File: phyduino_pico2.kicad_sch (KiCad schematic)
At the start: 7 parts, among them J2 PM2.54-1*8, J3 PM2.54-1*10, J4 PM2.54-1*6, J5 PM2.54-1*8, J7 HC-FPC-0.5-22P-CSH20

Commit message: Built board without USB-PD variant. Not yet complete.
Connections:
- net Microcontroller/HS_I2C0_SCL renamed Microcontroller/HS_I2C1_SCL
- net Microcontroller/HS_I2C0_SDA renamed Microcontroller/HS_I2C1_SDA
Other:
- sheet Microcontroller ports: added HS_I2C1_SCL, HS_I2C1_SDA; removed HS_I2C0_SCL, HS_I2C0_SDA
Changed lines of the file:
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@@
+			)
+		)
+		(property "Tolerance" ""
+			(at 300.99 256.54 0)
+			(hide yes)
+			(show_name no)
+			(do_not_autoplace no)
+			(effects
+				(font
+					(size 1.27 1.27)
+				)
 			)
 		)
@@
 			)
 		)
+		(property "Tolerance" ""
+			(at 295.91 256.54 0)
+			(hide yes)
+			(show_name no)
+			(do_not_autoplace no)
+			(effects
+				(font
+					(size 1.27 1.27)
+				)
+			)
+		)
 		(instances
 			(project "phyduino_pico2"
@@
 			)
 		)
+		(property "Tolerance" ""
+			(at 237.49 87.63 0)
+			(hide yes)
+			(show_name no)
+			(do_not_autoplace no)
+			(effects
+				(font
+					(size 1.27 1.27)
+				)
+			)
+		)
 		(pin "1"
 		)
@@
 			)
 		)
+		(property "Tolerance" ""
+			(at 237.49 137.16 0)
+			(hide yes)
+			(show_name no)
+			(do_not_autoplace no)
+			(effects
+				(font
+					(size 1.27 1.27)
+				)
+			)
+		)
 		(pin "13"
 		)
@@
 		)
 		(property "KiLib_Generator" "connector/pin_header_socket"
+			(at 237.49 62.23 0)
+			(hide yes)
+			(show_name no)
+			(do_not_autoplace no)
+			(effects
+				(font
+					(size 1.27 1.27)
+				)
+			)
+		)
+		(property "Tolerance" ""
 			(at 237.49 62.23 0)
 			(hide yes)
@@
 		)
 		(property "KiLib_Generator" "connector/pin_header_socket"
+			(at 40.64 62.23 0)
+			(hide yes)
+			(show_name no)
+			(do_not_autoplace no)
+			(effects
+				(font
+					(size 1.27 1.27)
+				)
+			)
+		)
+		(property "Tolerance" ""
 			(at 40.64 62.23 0)
 			(hide yes)
@@
 			)
 		)
+		(property "Tolerance" ""
+			(at 237.49 181.61 0)
+			(hide yes)
+			(show_name no)
+			(do_not_autoplace no)
+			(effects
+				(font
+					(size 1.27 1.27)
+				)
+			)
+		)
 		(pin "1"
 		)
@@
 			)
 		)
-		(pin "HS_I2C0_SCL" bidirectional
+		(pin "HS_I2C1_SCL" bidirectional
 			(at 143.51 116.84 0)
 			(effects
@@
 			)
 		)
-		(pin "HS_I2C0_SDA" bidirectional
+		(pin "HS_I2C1_SDA" bidirectional
 			(at 143.51 114.3 0)
 			(effects
@@
 			)
 		)
-		(pin "WIFI_UART_CTS" output
+		(pin "WIFI_UART_CTS" input
 			(at 107.95 179.07 180)
 			(effects
@@
 			)
 		)
-		(pin "WIFI_UART_RTS" input
+		(pin "WIFI_UART_RTS" output
 			(at 107.95 181.61 180)
 			(effects

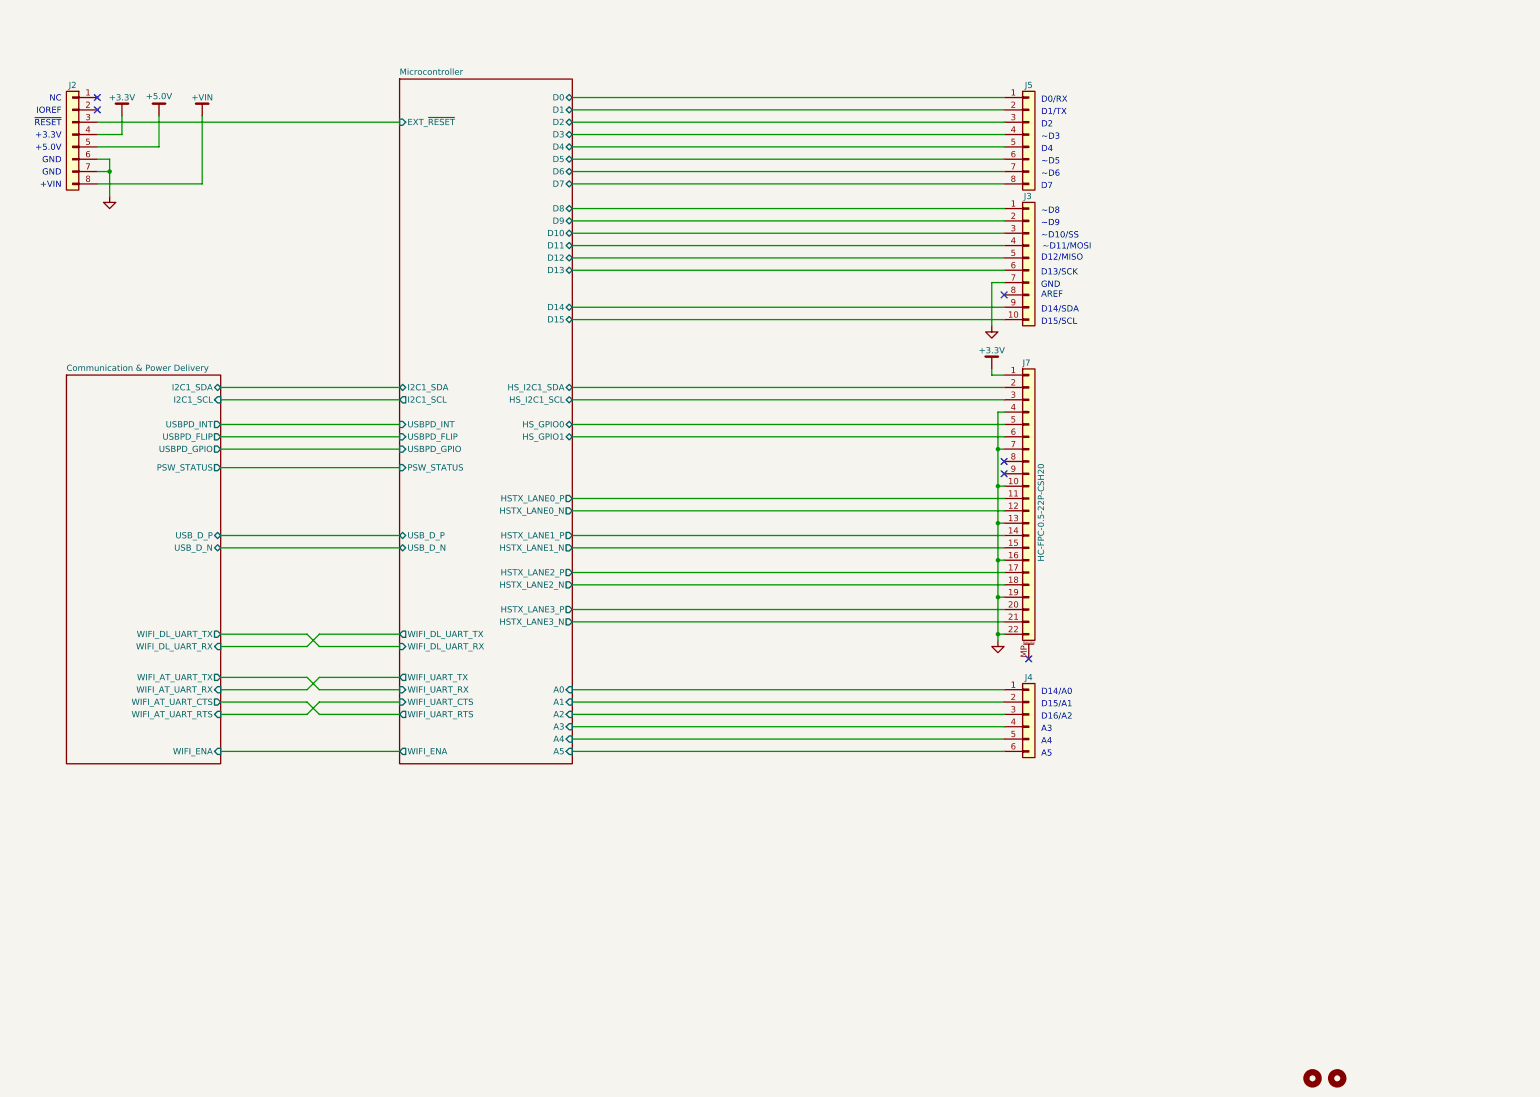
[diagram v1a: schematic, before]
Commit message: Development update : Changed the power input and tree, removed led for communication status.
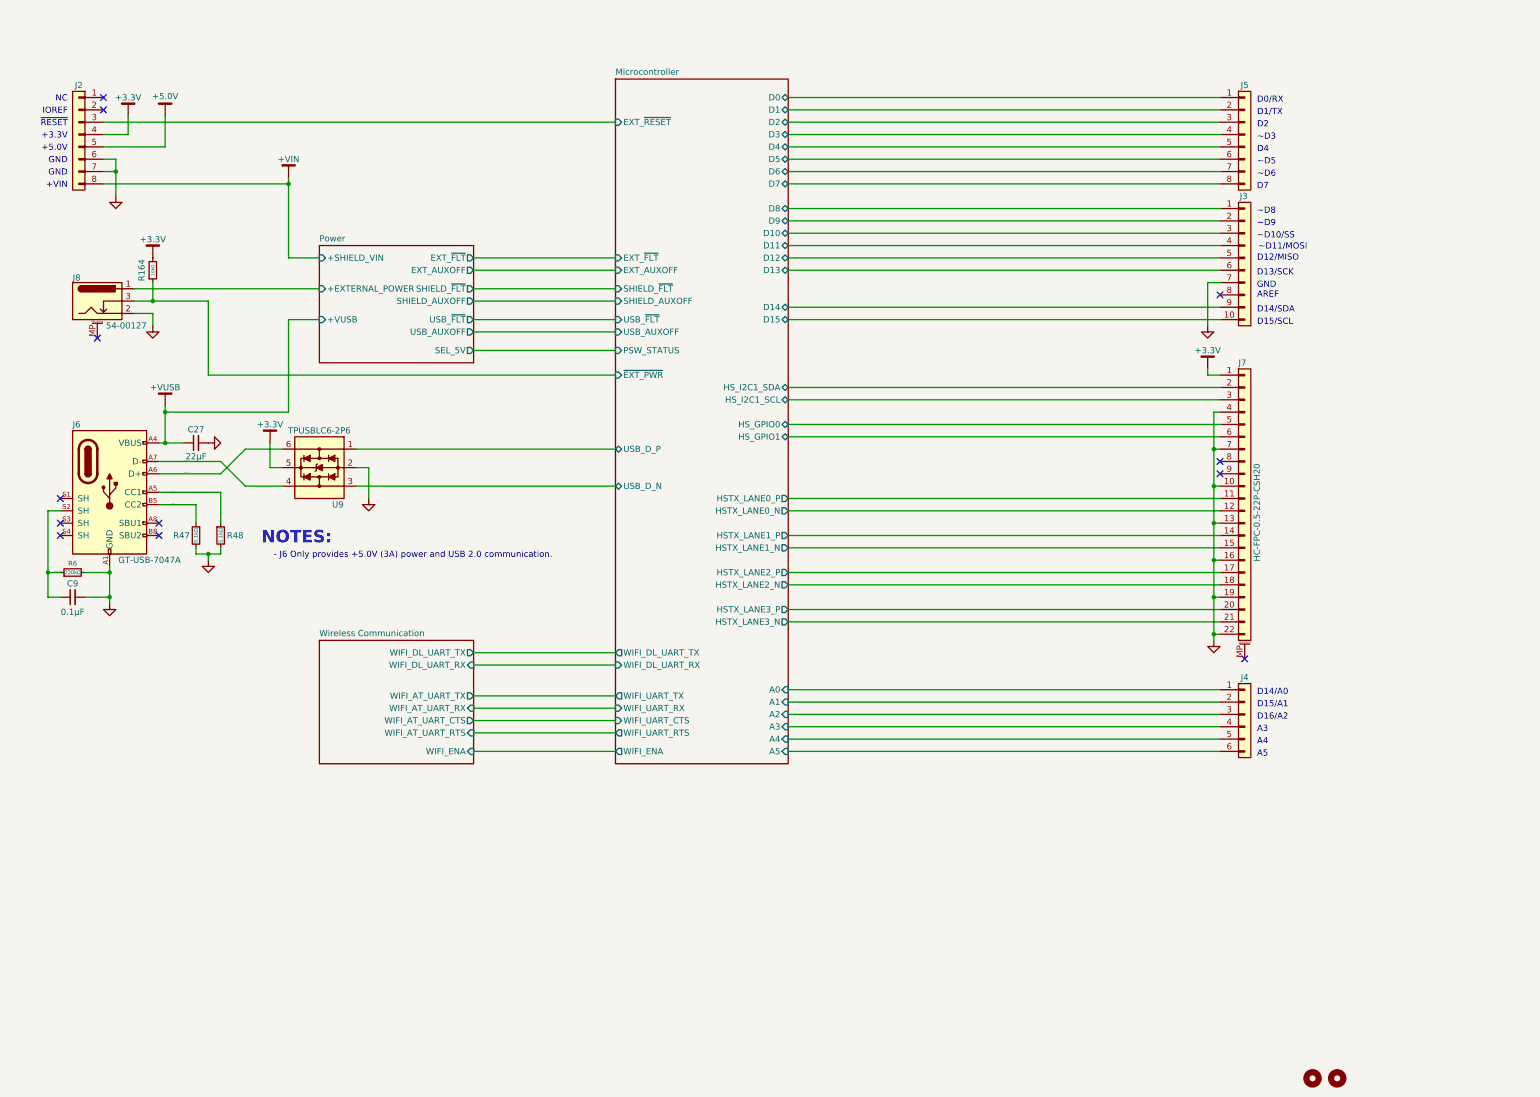
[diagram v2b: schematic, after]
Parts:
- added C27: 22µF, Capacitor_SMD:C_0805_2012Metric_Pad1.18x1.45mm_HandSolder, symbol Component - Device [KL]:C_Small
- added C9: 0.1µF, Capacitor_SMD:C_1206_3216Metric_Pad1.33x1.80mm_HandSolder, symbol Component - Device [KL]:C_Small
- added J6: GT-USB-7047A, Connector - PC SMT [UL]:GCT-USBC-GCT_USB4110, symbol KL - Connector:USB_C_Receptacle_USB2.0_16P
- added J8: 54-00127, Conector - Power [UL]:TENSILITY_54-00127, symbol [UL] Connector - Power Entry:Barrel_Jack_Tensility_54-00127
- added R164: 10kΩ, Resistor_SMD:R_0402_1005Metric, symbol Device:R_Small
- added R47, R48: 5.1kΩ, Resistor_SMD:R_0402_1005Metric, symbol phyduino_pico:R_Small
- added R6: 220kΩ, Resistor_SMD:R_0805_2012Metric_Pad1.20x1.40mm_HandSolder, symbol Component - Device [KL]:R_Small
- added U9: TPUSBLC6-2P6, Package_TO_SOT_SMD:SOT-666, symbol Protection - Signal:USBLC6-2P6
- J7: Variant (none) -> STUDENT
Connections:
- net +3.3V: now also R164.2, U9.5 (VBUS)
- net GND: now also C27.2, C9.2, J6.A1 (GND), J6.A12 (GND), J6.B1 (GND), J6.B12 (GND), J8.2, R47.2, R48.2, R6.2, U9.2 (GND)
- new net +VUSB: C27.1, J6.A4 (VBUS), J6.A9 (VBUS), J6.B4 (VBUS), J6.B9 (VBUS)
- new net Microcontroller/USB_D_N: U9.3 (I/O2)
- new net Microcontroller/USB_D_P: U9.1 (I/O1)
- new net Microcontroller/~{EXT_PWR}: J8.3, R164.1
- new net Power/+EXTERNAL_POWER: J8.1
- new net USB_CC1: J6.A5 (CC1), R48.1
- new net USB_CC2: J6.B5 (CC2), R47.1
- new net USB_COM_D_N: J6.A7 (D-), J6.B7 (D-), U9.4 (I/O2)
- new net USB_COM_D_P: J6.A6 (D+), J6.B6 (D+), U9.6 (I/O1)
- new net USB_COM_SHIELD: C9.1, J6.S2 (SH), R6.1
- no-connect marks 6 -> 12
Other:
- sheet Communication & Power Delivery renamed Wireless Communication
- added sheet Power (phyduino2_power_regs.kicad_sch)
- sheet Microcontroller ports: added EXT_AUXOFF, EXT_~{FLT}, SHIELD_AUXOFF, SHIELD_~{FLT}, USB_AUXOFF, USB_~{FLT}, ~{EXT_PWR}; removed I2C1_SCL, I2C1_SDA, USBPD_FLIP, USBPD_GPIO, USBPD_INT
- sheet Wireless Communication ports: added none; removed I2C1_SCL, I2C1_SDA, PSW_STATUS, USBPD_FLIP, USBPD_GPIO, USBPD_INT, USB_D_N, USB_D_P
- note added: "- J6 Only provides +5.0V (3A) power and USB 2.0 communication."
- note added: "NOTES:"
- moved on the sheet: J2, J3, J4, J5, J7

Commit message: Development update : Initial design review changes and PCB routing.
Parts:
- removed H1: MountingHole, MountingHole [KL]:MountingHole_3.2mm_M3, symbol Mechanical:MountingHole
- added J9: SM04B-SRSS-TB, Connector_JST:JST_SH_SM04B-SRSS-TB_1x04-1MP_P1.00mm_Horizontal, symbol Connector_Generic:Conn_01x04
- J2, J5: value PM2.54-1*8 -> PPPC081LFBN-RC; DIGIKEY PN 952-1823-ND -> (none); DIGKEY MANUFACTURER Harwin Inc. -> (none); KiLib_Generator connector/pin_header_socket -> (none); LCSC MANUFACTURER ZHOURI -> (none); LCSC PN C5224027 -> (none)
- J3: value PM2.54-1*10 -> PPPC101LFBN-RC; DIGIKEY PN 952-1846-ND -> (none); DIGKEY MANUFACTURER Harwin Inc. -> (none); KiLib_Generator connector/pin_header_socket -> (none); LCSC MANUFACTURER ZHOURI -> (none); LCSC PN C5116489 -> (none)
- J4: value PM2.54-1*6 -> PPPC061LFBN-RC; DIGIKEY PN 952-1808-ND -> (none); DIGKEY MANUFACTURER Harwin Inc. -> (none); KiLib_Generator connector/pin_header_socket -> (none); LCSC MANUFACTURER ZHOURI -> (none); LCSC PN C5224026 -> (none)
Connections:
- net +3.3V: now also J2.2 (Pin_2), J9.1 (Pin_1)
- net GND: now also J9.4 (Pin_4)
- net Microcontroller/D14: now also J9.2 (Pin_2)
- net Microcontroller/D15: now also J9.3 (Pin_3)
- net +VIN renamed +V_{IN}
- net +VUSB renamed +V_{USB}
- net Power/+EXTERNAL_POWER renamed +V_{EXTERNAL}
- no-connect marks 12 -> 11
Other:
- sheet Microcontroller ports: added WIFI_BOOT1; removed none
- sheet Wireless Communication ports: added WIFI_BOOT1; removed none
- moved on the sheet: C27, C9, J2, J3, J4, J5, J6, J7, J8, R164, R47, R48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
